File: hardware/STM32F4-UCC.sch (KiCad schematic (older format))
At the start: 36 parts, among them J2 STM32F4_Discovery_Header, SW1 BT1, SW2 BT2, SW3 BT3, SW4 BT4, U1 PLCC4

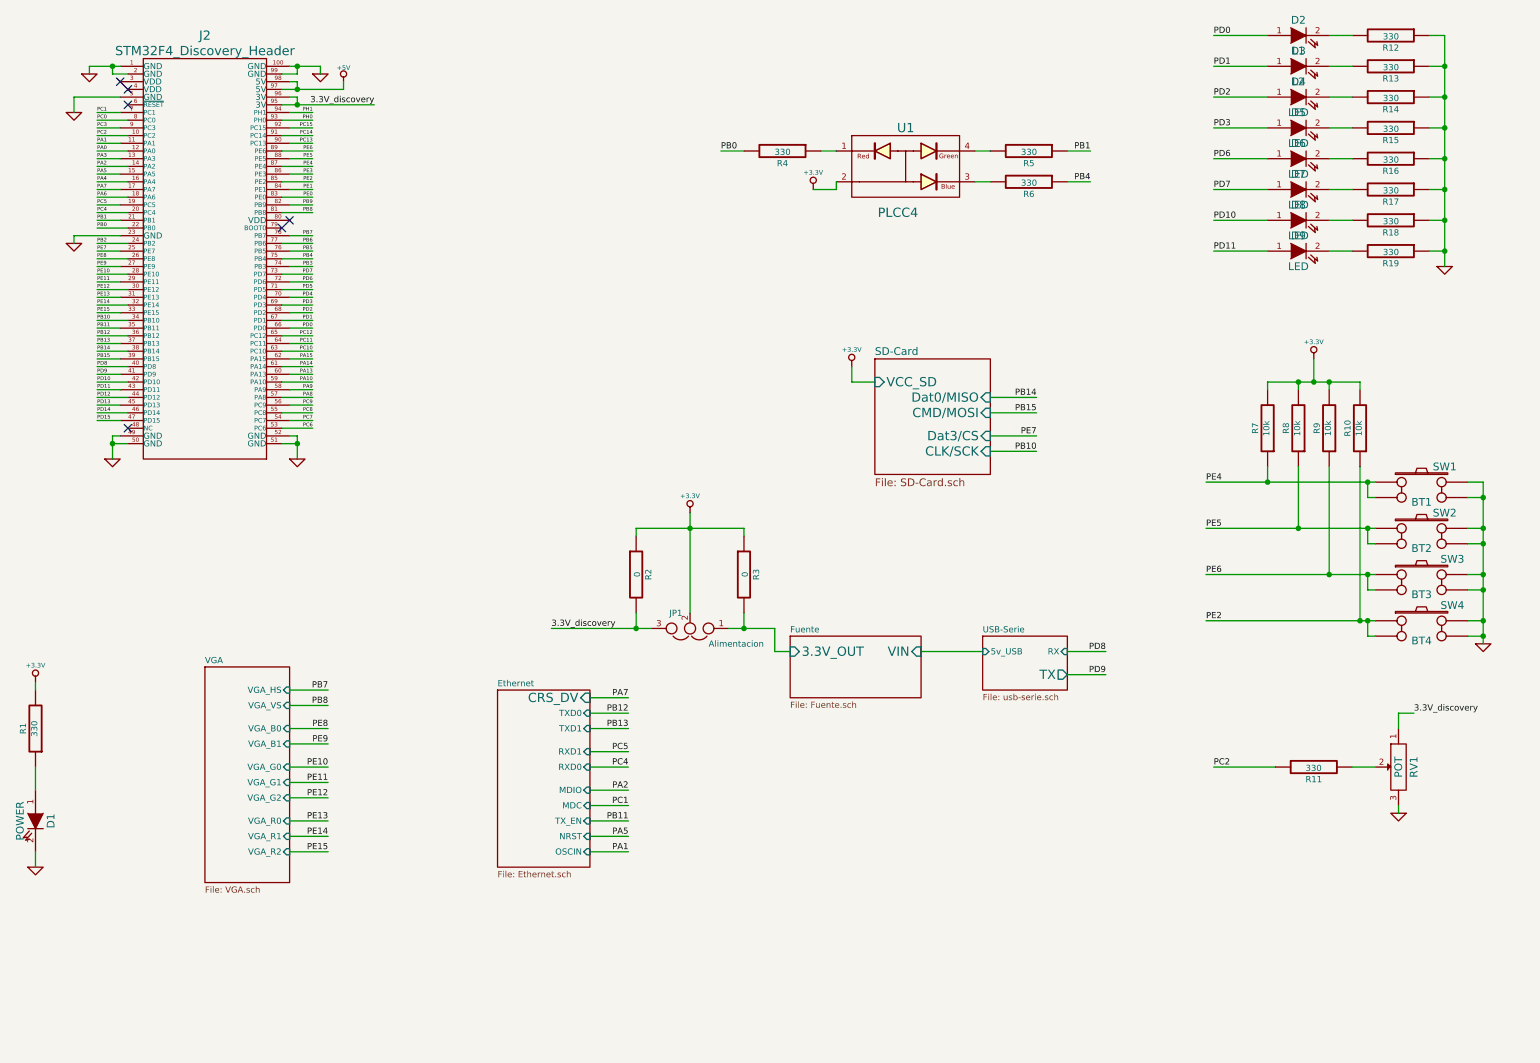
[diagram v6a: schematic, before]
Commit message: Placa terminada, serigrafia verificada, logos agregados
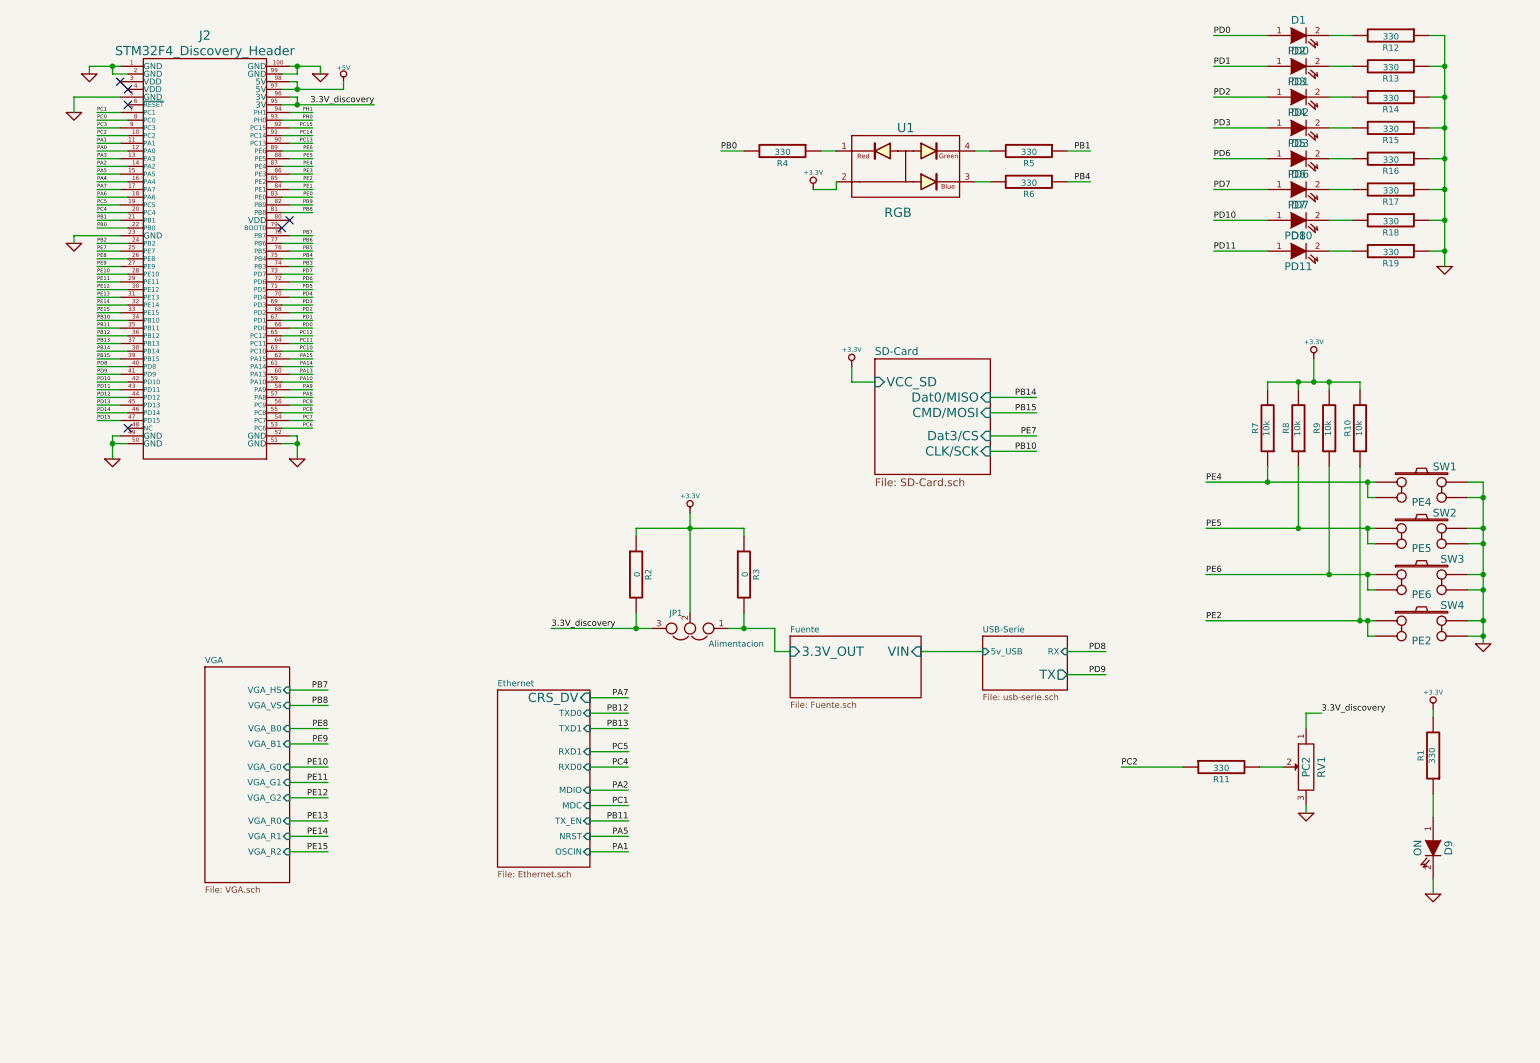
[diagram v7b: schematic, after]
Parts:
- D1: renamed from D2; value L1 -> PD0; footprint LEDs:LED-0805 -> w_Connectors:Led_0805
- D2: renamed from D3; value L2 -> PD1; footprint LEDs:LED-0805 -> w_Connectors:Led_0805
- D3: renamed from D4; value LED -> PD2; footprint LEDs:LED-0805 -> w_Connectors:Led_0805
- D4: renamed from D5; value LED -> PD3; footprint LEDs:LED-0805 -> w_Connectors:Led_0805
- D5: renamed from D6; value LED -> PD6; footprint LEDs:LED-0805 -> w_Connectors:Led_0805
- D6: renamed from D7; value LED -> PD7; footprint LEDs:LED-0805 -> w_Connectors:Led_0805
- D7: renamed from D8; value LED -> PD10; footprint LEDs:LED-0805 -> w_Connectors:Led_0805
- D8: renamed from D9; value LED -> PD11; footprint LEDs:LED-0805 -> w_Connectors:Led_0805
- D9: renamed from D1; value POWER -> ON; footprint LEDs:LED-0805 -> w_Connectors:Led_0805
- RV1: value POT -> PC2
- SW1: value BT1 -> PE4
- SW2: value BT2 -> PE5
- SW3: value BT3 -> PE6
- SW4: value BT4 -> PE2
- U1: value PLCC4 -> RGB
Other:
- moved on the sheet: D9, R1, R11, RV1
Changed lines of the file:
@@
 $EndComp
 $Comp
-L LED D2
+L LED D1
 U 1 1 538F871F
 P 9400 800
-F 0 "D2" H 9400 900 50  0000 C CNN
-F 1 "L1" H 9400 700 50  0000 C CNN
-F 2 "LEDs:LED-0805" H 9400 800 60  0001 C CNN
+F 0 "D1" H 9400 900 50  0000 C CNN
+F 1 "PD0" H 9400 700 50  0000 C CNN
+F 2 "w_Connectors:Led_0805" H 9400 800 60  0001 C CNN
 F 3 "" H 9400 800 60  0000 C CNN
 	1    9400 800
@@
 $EndComp
 $Comp
-L LED D3
+L LED D2
 U 1 1 538F87EC
 P 9400 1000
-F 0 "D3" H 9400 1100 50  0000 C CNN
-F 1 "L2" H 9400 900 50  0000 C CNN
-F 2 "LEDs:LED-0805" H 9400 1000 60  0001 C CNN
+F 0 "D2" H 9400 1100 50  0000 C CNN
+F 1 "PD1" H 9400 900 50  0000 C CNN
+F 2 "w_Connectors:Led_0805" H 9400 1000 60  0001 C CNN
 F 3 "" H 9400 1000 60  0000 C CNN
 	1    9400 1000
@@
 $EndComp
 $Comp
-L LED D4
+L LED D3
 U 1 1 538F8898
 P 9400 1200
-F 0 "D4" H 9400 1300 50  0000 C CNN
-F 1 "LED" H 9400 1100 50  0000 C CNN
-F 2 "LEDs:LED-0805" H 9400 1200 60  0001 C CNN
+F 0 "D3" H 9400 1300 50  0000 C CNN
+F 1 "PD2" H 9400 1100 50  0000 C CNN
+F 2 "w_Connectors:Led_0805" H 9400 1200 60  0001 C CNN
 F 3 "" H 9400 1200 60  0000 C CNN
 	1    9400 1200
@@
 $EndComp
 $Comp
-L LED D5
+L LED D4
 U 1 1 538F889E
 P 9400 1400
-F 0 "D5" H 9400 1500 50  0000 C CNN
-F 1 "LED" H 9400 1300 50  0000 C CNN
-F 2 "LEDs:LED-0805" H 9400 1400 60  0001 C CNN
+F 0 "D4" H 9400 1500 50  0000 C CNN
+F 1 "PD3" H 9400 1300 50  0000 C CNN
+F 2 "w_Connectors:Led_0805" H 9400 1400 60  0001 C CNN
 F 3 "" H 9400 1400 60  0000 C CNN
 	1    9400 1400
@@
 $EndComp
 $Comp
-L LED D6
+L LED D5
 U 1 1 538F8960
 P 9400 1600
-F 0 "D6" H 9400 1700 50  0000 C CNN
-F 1 "LED" H 9400 1500 50  0000 C CNN
-F 2 "LEDs:LED-0805" H 9400 1600 60  0001 C CNN
+F 0 "D5" H 9400 1700 50  0000 C CNN
+F 1 "PD6" H 9400 1500 50  0000 C CNN
+F 2 "w_Connectors:Led_0805" H 9400 1600 60  0001 C CNN
 F 3 "" H 9400 1600 60  0000 C CNN
 	1    9400 1600
@@
 $EndComp
 $Comp
-L LED D7
+L LED D6
 U 1 1 538F8966
 P 9400 1800
-F 0 "D7" H 9400 1900 50  0000 C CNN
-F 1 "LED" H 9400 1700 50  0000 C CNN
-F 2 "LEDs:LED-0805" H 9400 1800 60  0001 C CNN
+F 0 "D6" H 9400 1900 50  0000 C CNN
+F 1 "PD7" H 9400 1700 50  0000 C CNN
+F 2 "w_Connectors:Led_0805" H 9400 1800 60  0001 C CNN
 F 3 "" H 9400 1800 60  0000 C CNN
 	1    9400 1800
@@
 $EndComp
 $Comp
-L LED D8
+L LED D7
 U 1 1 538F896C
 P 9400 2000
-F 0 "D8" H 9400 2100 50  0000 C CNN
-F 1 "LED" H 9400 1900 50  0000 C CNN
-F 2 "LEDs:LED-0805" H 9400 2000 60  0001 C CNN
+F 0 "D7" H 9400 2100 50  0000 C CNN
+F 1 "PD10" H 9400 1900 50  0000 C CNN
+F 2 "w_Connectors:Led_0805" H 9400 2000 60  0001 C CNN
 F 3 "" H 9400 2000 60  0000 C CNN
 	1    9400 2000
@@
 $EndComp
 $Comp
-L LED D9
+L LED D8
 U 1 1 538F8972
 P 9400 2200
-F 0 "D9" H 9400 2300 50  0000 C CNN
-F 1 "LED" H 9400 2100 50  0000 C CNN
-F 2 "LEDs:LED-0805" H 9400 2200 60  0001 C CNN
+F 0 "D8" H 9400 2300 50  0000 C CNN
+F 1 "PD11" H 9400 2100 50  0000 C CNN
+F 2 "w_Connectors:Led_0805" H 9400 2200 60  0001 C CNN
 F 3 "" H 9400 2200 60  0000 C CNN
 	1    9400 2200
@@
 P 10200 3750
 F 0 "SW1" H 10350 3900 50  0000 C CNN
-F 1 "BT1" H 10200 3670 50  0000 C CNN
+F 1 "PE4" H 10200 3670 50  0000 C CNN
 F 2 "w_switch:PCB_PUSH" H 10200 3750 60  0001 C CNN
 F 3 "" H 10200 3750 60  0000 C CNN
@@
 P 10200 4050
 F 0 "SW2" H 10350 4200 50  0000 C CNN
-F 1 "BT2" H 10200 3970 50  0000 C CNN
+F 1 "PE5" H 10200 3970 50  0000 C CNN
 F 2 "w_switch:PCB_PUSH" H 10200 4050 60  0001 C CNN
 F 3 "" H 10200 4050 60  0000 C CNN
@@
 P 10200 4350
 F 0 "SW3" H 10400 4500 50  0000 C CNN
-F 1 "BT3" H 10200 4270 50  0000 C CNN
+F 1 "PE6" H 10200 4270 50  0000 C CNN
 F 2 "w_switch:PCB_PUSH" H 10200 4350 60  0001 C CNN
 F 3 "" H 10200 4350 60  0000 C CNN
@@
 P 10200 4650
 F 0 "SW4" H 10400 4800 50  0000 C CNN
-F 1 "BT4" H 10200 4570 50  0000 C CNN
+F 1 "PE2" H 10200 4570 50  0000 C CNN
 F 2 "w_switch:PCB_PUSH" H 10200 4650 60  0001 C CNN
 F 3 "" H 10200 4650 60  0000 C CNN
@@
 L POT RV1
 U 1 1 538FDDAB
-P 10050 5550
-F 0 "RV1" H 10050 5450 50  0000 C CNN
-F 1 "POT" H 10050 5550 50  0000 C CNN
-F 2 "w_Connectors:POTE" H 10050 5550 60  0001 C CNN
-F 3 "" H 10050 5550 60  0000 C CNN
-	1    10050 5550
+P 9450 5550
+F 0 "RV1" H 9450 5450 50  0000 C CNN
+F 1 "PC2" H 9450 5550 50  0000 C CNN
+F 2 "w_Connectors:POTE" H 9450 5550 60  0001 C CNN
+F 3 "" H 9450 5550 60  0000 C CNN
+	1    9450 5550
 	0    -1   1    0
 $EndComp
@@
 L GND #PWR04
 U 1 1 538FE083
-P 10050 5850
-F 0 "#PWR04" H 10050 5850 30  0001 C CNN
-F 1 "GND" H 10050 5780 30  0001 C CNN
-F 2 "" H 10050 5850 60  0000 C CNN
-F 3 "" H 10050 5850 60  0000 C CNN
-	1    10050 5850
+P 9450 5850
+F 0 "#PWR04" H 9450 5850 30  0001 C CNN
+F 1 "GND" H 9450 5780 30  0001 C CNN
+F 2 "" H 9450 5850 60  0000 C CNN
+F 3 "" H 9450 5850 60  0000 C CNN
+	1    9450 5850
 	-1   0    0    -1
 $EndComp
@@
 L R R11
 U 1 1 538FE166
-P 9500 5550
-F 0 "R11" V 9580 5550 40  0000 C CNN
-F 1 "330" V 9507 5551 40  0000 C CNN
-F 2 "Resistors_SMD:R_0805" V 9430 5550 30  0001 C CNN
-F 3 "" H 9500 5550 30  0000 C CNN
-	1    9500 5550
+P 8900 5550
+F 0 "R11" V 8980 5550 40  0000 C CNN
+F 1 "330" V 8907 5551 40  0000 C CNN
+F 2 "Resistors_SMD:R_0805" V 8830 5550 30  0001 C CNN
+F 3 "" H 8900 5550 30  0000 C CNN
+	1    8900 5550
 	0    -1   1    0
 $EndComp
@@
 Connection ~ 9500 3050
 Wire Wire Line
-	10050 5850 10050 5800
-Wire Wire Line
-	9900 5550 9750 5550
-Wire Wire Line
-	10050 5200 10050 5300
-Wire Wire Line
-	9250 5550 8850 5550
+	9450 5850 9450 5800
+Wire Wire Line
+	9300 5550 9150 5550
+Wire Wire Line
+	9450 5200 9450 5300
+Wire Wire Line
+	8650 5550 8250 5550
 Wire Wire Line
 	5800 1550 5650 1550
@@
 Wire Wire Line
 	7350 4800 6950 4800
-Text Label 10150 5200 0    40   ~ 0
+Text Label 9550 5200 0    40   ~ 0
 3.3V_discovery
 Wire Wire Line
-	10050 5200 10150 5200
+	9450 5200 9550 5200
 Wire Wire Line
 	8150 4950 7900 4950
@@
 Text Label 3100 5150 2    40   ~ 0
 PB8
-Text Label 8850 5550 0    40   ~ 0
+Text Label 8250 5550 0    40   ~ 0
 PC2
 Text Label 8800 3700 0    40   ~ 0
@@
 PA7
 $Comp
-L LED D1
+L LED D9
 U 1 1 53E67E0F
-P 1200 5900
-F 0 "D1" H 1200 6000 50  0000 C CNN
-F 1 "POWER" H 1200 5800 50  0000 C CNN
-F 2 "LEDs:LED-0805" H 1200 5900 60  0001 C CNN
-F 3 "" H 1200 5900 60  0000 C CNN
-	1    1200 5900
+P 10275 6075
+F 0 "D9" H 10275 6175 50  0000 C CNN
+F 1 "ON" H 10275 5975 50  0000 C CNN
+F 2 "w_Connectors:Led_0805" H 10275 6075 60  0001 C CNN
+F 3 "" H 10275 6075 60  0000 C CNN
+	1    10275 6075
 	0    1    1    0
 $EndComp
@@
 L R R1
 U 1 1 53E67E15
-P 1200 5300
-F 0 "R1" V 1280 5300 40  0000 C CNN
-F 1 "330" V 1207 5301 40  0000 C CNN
-F 2 "Resistors_SMD:R_0805" V 1130 5300 30  0001 C CNN
-F 3 "" H 1200 5300 30  0000 C CNN
-	1    1200 5300
+P 10275 5475
+F 0 "R1" V 10355 5475 40  0000 C CNN
+F 1 "330" V 10282 5476 40  0000 C CNN
+F 2 "Resistors_SMD:R_0805" V 10205 5475 30  0001 C CNN
+F 3 "" H 10275 5475 30  0000 C CNN
+	1    10275 5475
 	-1   0    0    1
 $EndComp
 Wire Wire Line
-	1200 6200 1200 6100
+	10275 6375 10275 6275
 $Comp
 L GND #PWR06
 U 1 1 53E67E7B
-P 1200 6200
-F 0 "#PWR06" H 1200 6200 30  0001 C CNN
-F 1 "GND" H 1200 6130 30  0001 C CNN
-F 2 "" H 1200 6200 60  0000 C CNN
-F 3 "" H 1200 6200 60  0000 C CNN
-	1    1200 6200
+P 10275 6375
+F 0 "#PWR06" H 10275 6375 30  0001 C CNN
+F 1 "GND" H 10275 6305 30  0001 C CNN
+F 2 "" H 10275 6375 60  0000 C CNN
+F 3 "" H 10275 6375 60  0000 C CNN
+	1    10275 6375
 	1    0    0    -1
 $EndComp
@@
 L +3.3V #PWR07
 U 1 1 53E6821B
-P 1200 5000
-F 0 "#PWR07" H 1200 4960 30  0001 C CNN
-F 1 "+3.3V" H 1200 5110 30  0000 C CNN
-F 2 "" H 1200 5000 60  0000 C CNN
-F 3 "" H 1200 5000 60  0000 C CNN
-	1    1200 5000
-	1    0    0    -1
-$EndComp
-Wire Wire Line
-	1200 5050 1200 5000
-Wire Wire Line
-	1200 5700 1200 5550
+P 10275 5175
+F 0 "#PWR07" H 10275 5135 30  0001 C CNN
+F 1 "+3.3V" H 10275 5285 30  0000 C CNN
+F 2 "" H 10275 5175 60  0000 C CNN
+F 3 "" H 10275 5175 60  0000 C CNN
+	1    10275 5175
+	1    0    0    -1
+$EndComp
+Wire Wire Line
+	10275 5225 10275 5175
+Wire Wire Line
+	10275 5875 10275 5725
 $Comp
 L JUMPER3 JP1
@@
 P 6850 1650
 F 0 "U1" H 6850 1900 60  0000 C CNN
-F 1 "PLCC4" H 6800 1350 60  0000 C CNN
+F 1 "RGB" H 6800 1350 60  0000 C CNN
 F 2 "w_Connectors:PLCC4" H 7050 1750 60  0001 C CNN
 F 3 "" H 7050 1750 60  0000 C CNN
